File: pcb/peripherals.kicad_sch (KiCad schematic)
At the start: 19 parts, among them J2 Conn_02x10_Odd_Even, U5 NRF24L01_Breakout, U7 BMI270, U8 HYCW110-TF10-180B

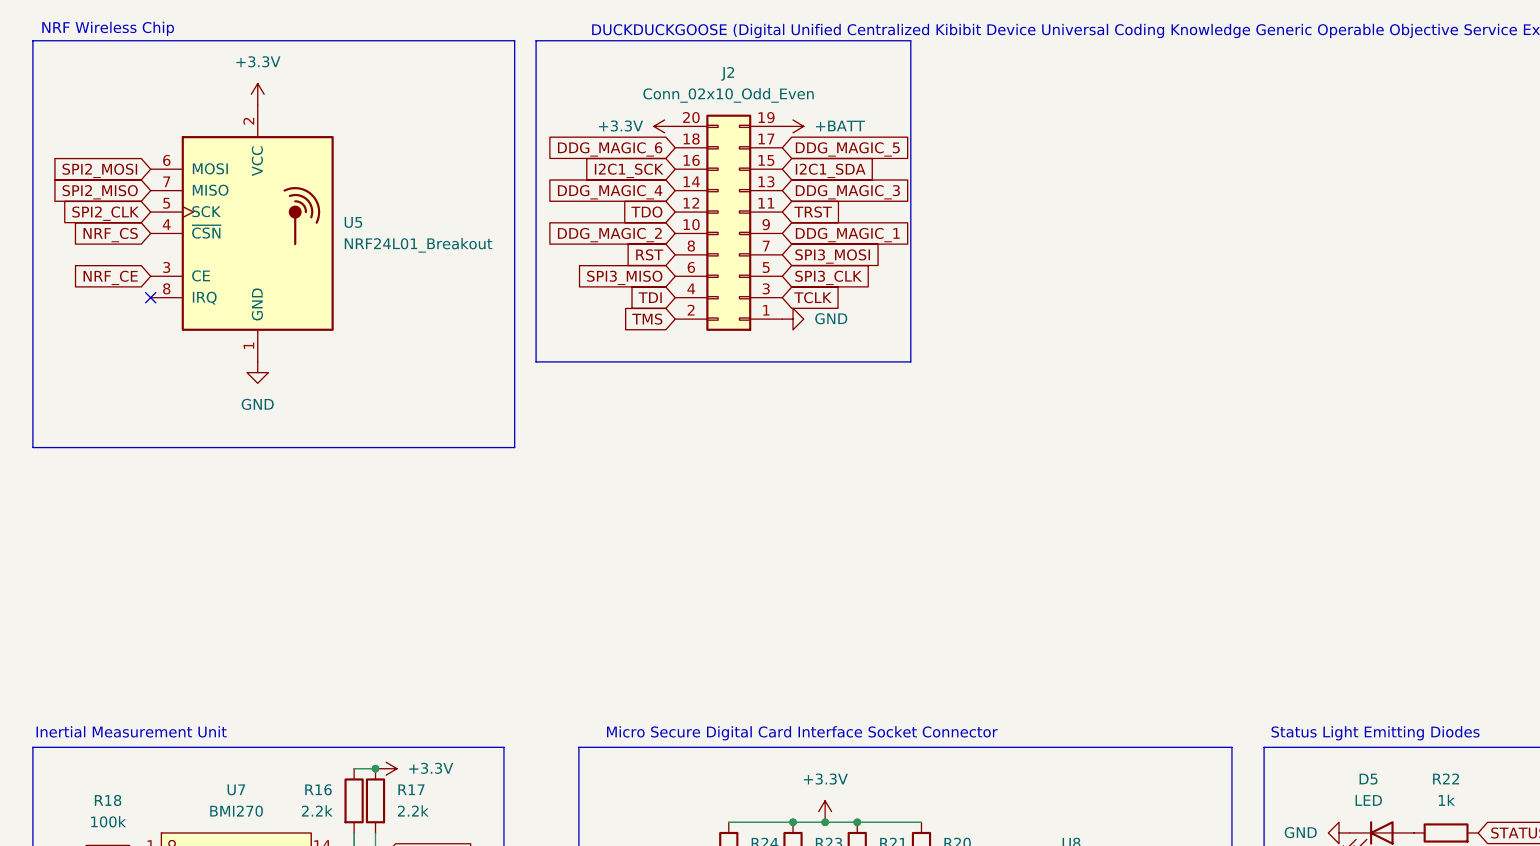
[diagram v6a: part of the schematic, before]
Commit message: [pcb] utilize unused gpios, silkscreen improvements and [journal] add entry for 7/9
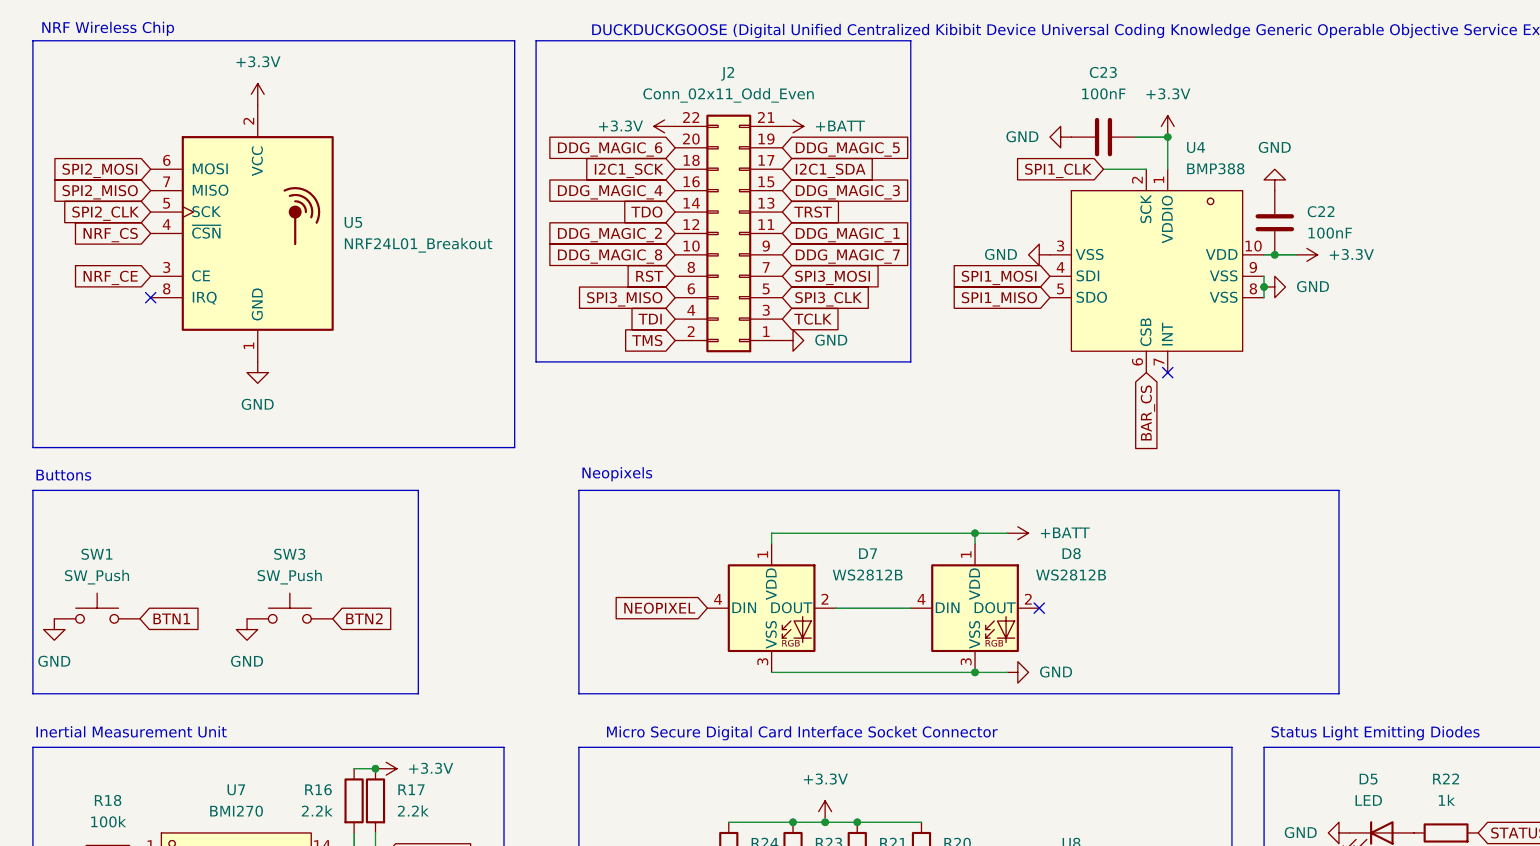
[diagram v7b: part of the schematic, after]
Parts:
- added C22, C23: 100nF, Capacitor_SMD:C_0805_2012Metric_Pad1.18x1.45mm_HandSolder, symbol Device:C
- added D7, D8: WS2812B, LED_SMD:LED_WS2812B_PLCC4_5.0x5.0mm_P3.2mm, symbol LED:WS2812B
- added SW1, SW3: SW_Push, lcsc:SW-SMD_L4.0-W2.9-LS5.0, symbol Switch:SW_Push
- added U4: BMP388, Package_LGA:ST_HLGA-10_2x2mm_P0.5mm_LayoutBorder3x2y, symbol lcsc:BMP388
- J2: value Conn_02x10_Odd_Even -> Conn_02x11_Odd_Even; footprint Connector_PinHeader_2.54mm:PinHeader_2x10_P2.54mm_Vertical -> Connector_PinHeader_2.54mm:PinHeader_2x11_P2.54mm_Vertical; symbol Connector_Generic:Conn_02x10_Odd_Even -> Connector_Generic:Conn_02x11_Odd_Even
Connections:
- net +3.3V: now also J2.22 (Pin_22), C22.2, C23.2, U4.1 (VDDIO), U4.10 (VDD); no longer J2.20 (Pin_20)
- net +BATT: now also J2.21 (Pin_21), D7.1 (VDD), D8.1 (VDD); no longer J2.19 (Pin_19)
- net DDG_MAGIC_1: now also J2.11 (Pin_11); no longer J2.9 (Pin_9)
- net DDG_MAGIC_2: now also J2.12 (Pin_12); no longer J2.10 (Pin_10)
- net DDG_MAGIC_3: now also J2.15 (Pin_15); no longer J2.13 (Pin_13)
- net DDG_MAGIC_4: now also J2.16 (Pin_16); no longer J2.14 (Pin_14)
- net DDG_MAGIC_5: now also J2.19 (Pin_19); no longer J2.17 (Pin_17)
- net DDG_MAGIC_6: now also J2.20 (Pin_20); no longer J2.18 (Pin_18)
- net GND: now also C22.1, C23.1, D7.3 (VSS), D8.3 (VSS), SW1.1, SW3.1, U4.3 (VSS), U4.8 (VSS), U4.9 (VSS)
- net I2C1_SCK: now also J2.18 (Pin_18); no longer J2.16 (Pin_16)
- net I2C1_SDA: now also J2.17 (Pin_17); no longer J2.15 (Pin_15)
- net TDO: now also J2.14 (Pin_14); no longer J2.12 (Pin_12)
- net TRST: now also J2.13 (Pin_13); no longer J2.11 (Pin_11)
- new net: D7.2 (DOUT), D8.4 (DIN)
- new net BAR_CS: U4.6 (CSB)
- new net BTN1: SW1.2
- new net BTN2: SW3.2
- new net DDG_MAGIC_7: J2.9 (Pin_9)
- new net DDG_MAGIC_8: J2.10 (Pin_10)
- new net NEOPIXEL: D7.4 (DIN)
- new net SPI1_CLK: U4.2 (SCK)
- new net SPI1_MISO: U4.5 (SDO)
- new net SPI1_MOSI: U4.4 (SDI)
- no-connect marks 7 -> 9
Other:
- note added: "Buttons"
- note added: "Neopixels"

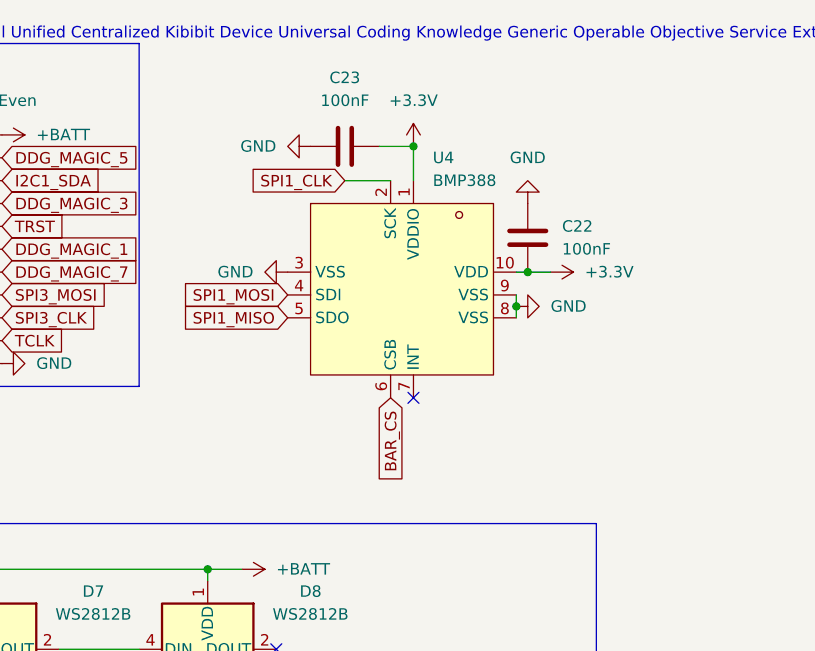
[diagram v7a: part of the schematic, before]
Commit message: [pcb] some more silkscreen improvements
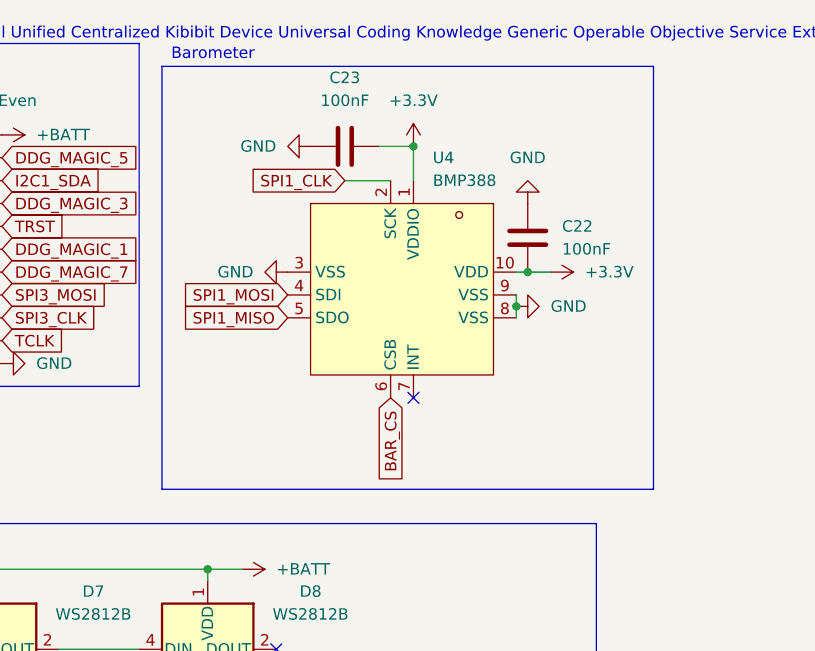
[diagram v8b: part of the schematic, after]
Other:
- note added: "Barometer"
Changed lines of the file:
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@@
+	)
+	(rectangle
+		(start 125.73 19.05)
+		(end 180.34 66.04)
+		(stroke
+			(width 0)
+			(type default)
+		)
+		(fill
+			(type none)
+		)
 	)
 	(rectangle
@@
 		)
 	)
+	(text "Barometer"
+		(exclude_from_sim no)
+		(at 126.746 17.78 0)
+		(effects
+			(font
+				(size 1.27 1.27)
+			)
+			(justify left)
+		)
+	)
